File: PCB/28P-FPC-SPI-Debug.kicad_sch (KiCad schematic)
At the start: 33 parts, among them J1 Conn_01x08, J3 SFV24R-1STBE1HLF, Q1 Si1308EDL, Q2 AO3401A, Q3 S8050, U1 RT9193-33GB, U2 TXB0108PW

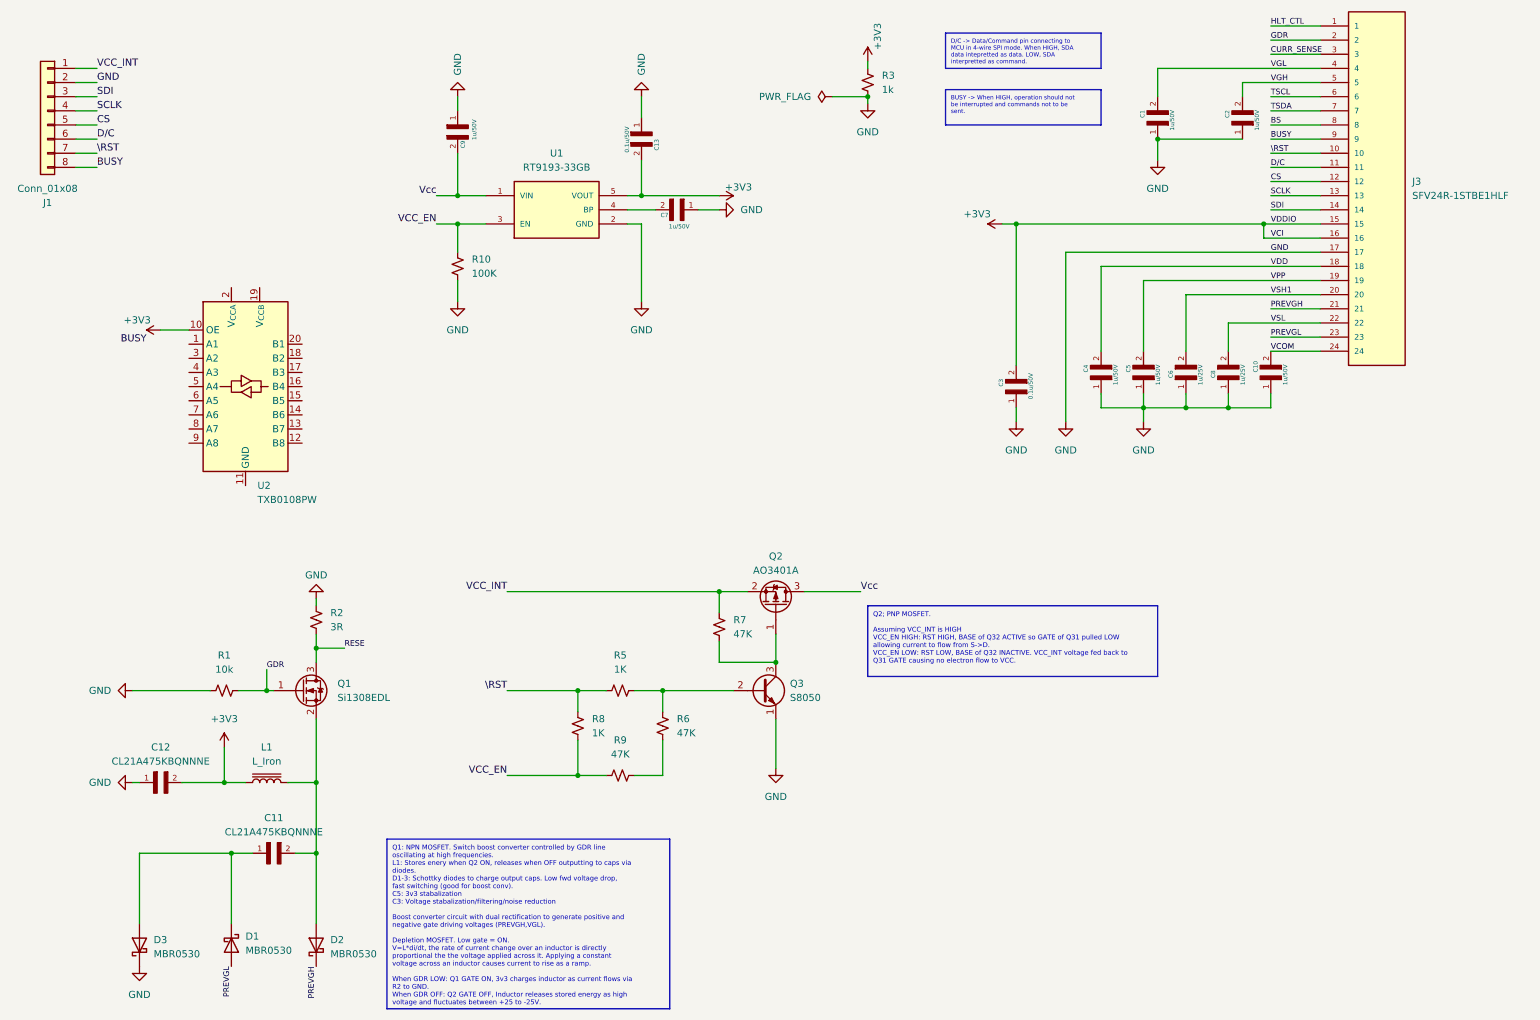
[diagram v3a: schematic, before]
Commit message: Added nets for TXB018PW. Resized PCB to size of 2.13in e-paper display with ~5mm excess on edges. Questionable part placement start.
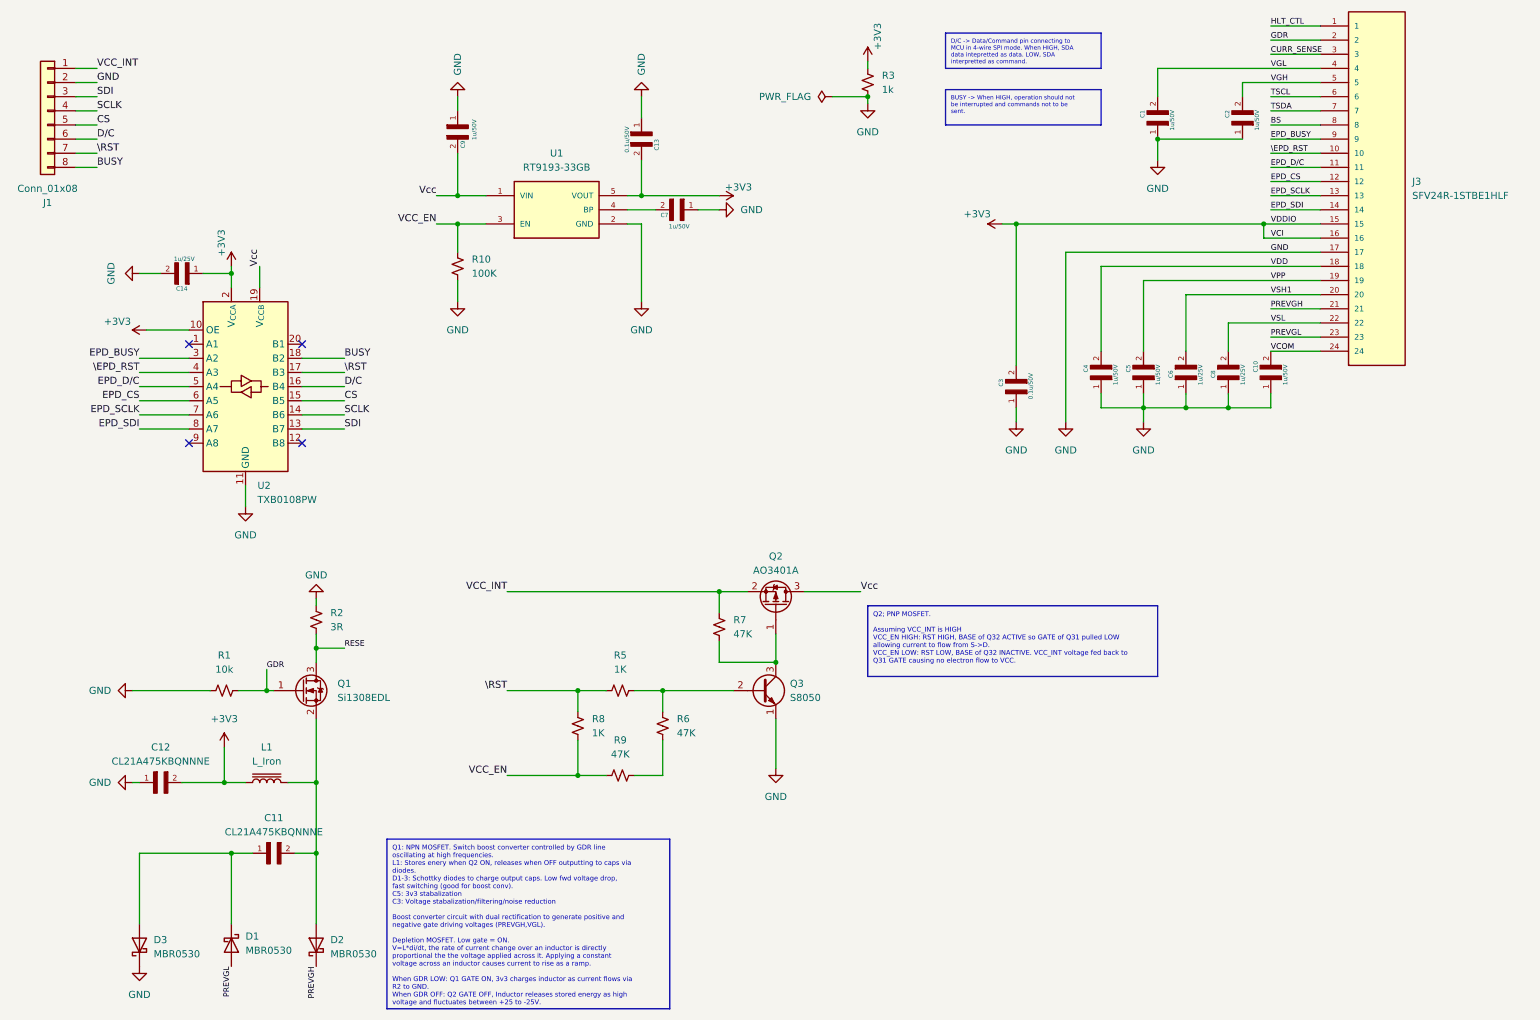
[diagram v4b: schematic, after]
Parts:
- added C14: 1u/25V, capacitors-cam:CAPC1608X90N, symbol Capacitors:CL10B105KA8NNNC
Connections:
- net +3V3: now also U2.2 (V_{CCA}), C14.1
- net BUSY: now also U2.18 (B2); no longer J3.9
- net CS: now also U2.15 (B5); no longer J3.12
- net D/C: now also U2.16 (B4); no longer J3.11
- net GND: now also U2.11 (GND), C14.2
- net SCLK: now also U2.14 (B6); no longer J3.13
- net SDI: now also U2.13 (B7); no longer J3.14
- net Vcc: now also U2.19 (V_{CCB})
- net \RST: now also U2.17 (B3); no longer J3.10
- net EPD_BUSY: now reaches U2.3 (A2)
- net EPD_BUSY: now also J3.9
- net \EPD_RST: now reaches U2.4 (A3)
- net \EPD_RST: now also J3.10
- net EPD_D/C: now reaches U2.5 (A4)
- net EPD_D/C: now also J3.11
- net EPD_CS: now reaches U2.6 (A5)
- net EPD_CS: now also J3.12
- net EPD_SCLK: now reaches U2.7 (A6)
- net EPD_SCLK: now also J3.13
- net EPD_SDI: now reaches U2.8 (A7)
- net EPD_SDI: now also J3.14
- no-connect marks 0 -> 4

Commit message: track placement
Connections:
- net VCC_EN: now also R9.1; no longer R9.2
- net VCC_INT: now also Q2.3 (D); no longer Q2.2 (S)
- net Vcc: now also Q2.2 (S); no longer Q2.3 (D)
- net at R6.1: now also R9.2; no longer R9.1
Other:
- moved on the sheet: Q2, R9
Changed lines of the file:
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@@
 	(symbol
 		(lib_id "Transistor_FET:AO3401A")
-		(at 149.86 120.65 270)
-		(mirror x)
-		(unit 1)
-		(exclude_from_sim no)
-		(in_bom yes)
-		(on_board yes)
-		(dnp no)
-		(fields_autoplaced yes)
+		(at 149.86 120.65 90)
+		(unit 1)
+		(exclude_from_sim no)
+		(in_bom yes)
+		(on_board yes)
+		(dnp no)
 		(property "Reference" "Q2"
 			(at 149.86 111.76 90)
@@
 		)
 		(property "Footprint" "Package_TO_SOT_SMD:SOT-23"
-			(at 147.955 115.57 0)
+			(at 151.765 115.57 0)
 			(effects
 				(font
@@
 		)
 		(property "Datasheet" "http://www.aosmd.com/pdfs/datasheet/AO3401A.pdf"
-			(at 146.05 115.57 0)
+			(at 153.67 115.57 0)
 			(effects
 				(font
@@
 	(symbol
 		(lib_id "Device:R_Small_US")
-		(at 121.92 151.13 270)
-		(unit 1)
-		(exclude_from_sim no)
-		(in_bom yes)
-		(on_board yes)
-		(dnp no)
-		(fields_autoplaced yes)
+		(at 121.92 151.13 90)
+		(mirror x)
+		(unit 1)
+		(exclude_from_sim no)
+		(in_bom yes)
+		(on_board yes)
+		(dnp no)
 		(property "Reference" "R9"
 			(at 121.92 144.78 90)

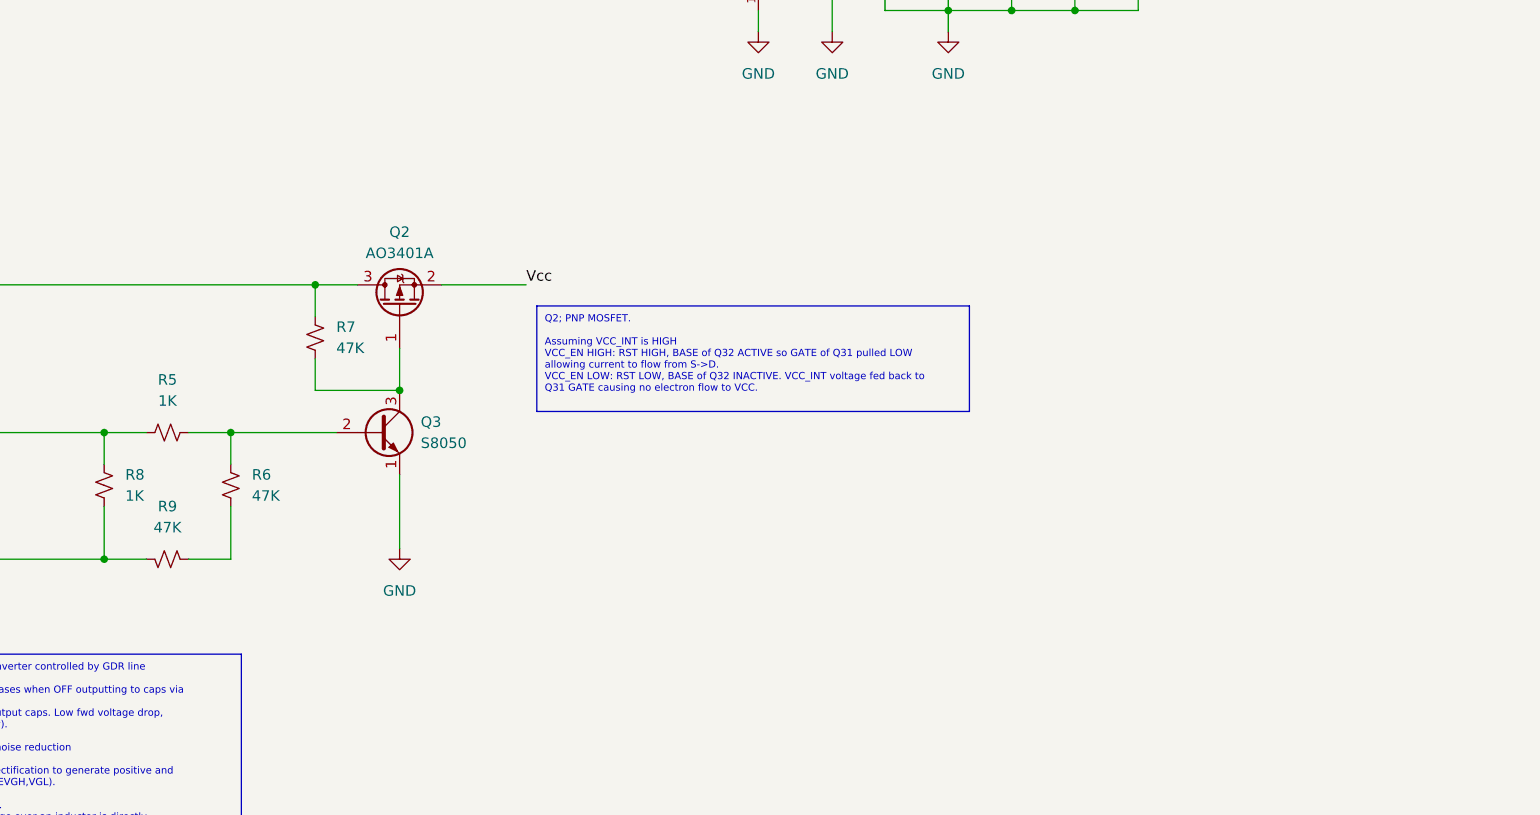
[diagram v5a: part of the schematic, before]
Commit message: Added breakout 28pin header for debugging. Track cleanup. Changed 0603 footprint due to clearance violations. Increased board size to fit header.
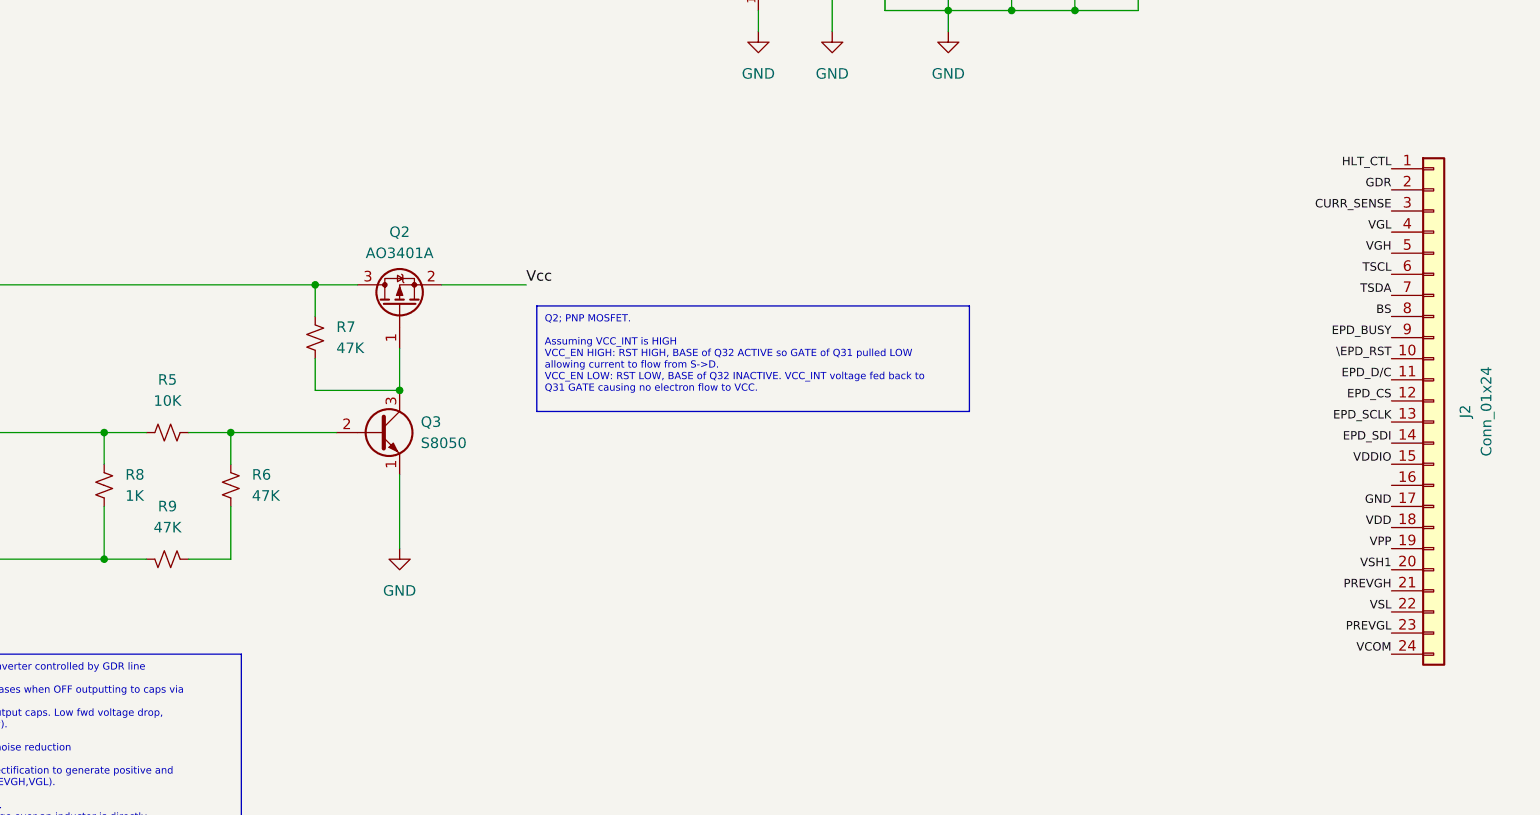
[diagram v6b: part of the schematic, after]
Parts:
- added J2: Conn_01x24, Connector_PinHeader_2.54mm:PinHeader_2x12_P2.54mm_Vertical, symbol Connector_Generic:Conn_01x24
- R1, R10, R2, R3, R6, R7, R8, R9: footprint Resistor_SMD:R_0201_0603Metric -> Resistor_SMD:R_0603_1608Metric_Pad0.98x0.95mm_HandSolder
- R5: value 1K -> 10K; footprint Resistor_SMD:R_0201_0603Metric -> Resistor_SMD:R_0603_1608Metric_Pad0.98x0.95mm_HandSolder
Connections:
- net +3V3: now also J2.15 (Pin_15)
- net BS: now also J2.8 (Pin_8)
- net CURR_SENSE: now also J2.3 (Pin_3)
- net EPD_BUSY: now also J2.9 (Pin_9)
- net EPD_CS: now also J2.12 (Pin_12)
- net EPD_D/C: now also J2.11 (Pin_11)
- net EPD_SCLK: now also J2.13 (Pin_13)
- net EPD_SDI: now also J2.14 (Pin_14)
- net GDR: now also J2.2 (Pin_2)
- net GND: now also J2.17 (Pin_17)
- net HLT_CTL: now also J2.1 (Pin_1)
- net PREVGH: now also J2.21 (Pin_21)
- net PREVGL: now also J2.23 (Pin_23)
- net TSCL: now also J2.6 (Pin_6)
- net TSDA: now also J2.7 (Pin_7)
- net VCOM: now also J2.24 (Pin_24)
- net VDD: now also J2.18 (Pin_18)
- net VGH: now also J2.5 (Pin_5)
- net VGL: now also J2.4 (Pin_4)
- net VPP: now also J2.19 (Pin_19)
- net VSH1: now also J2.20 (Pin_20)
- net VSL: now also J2.22 (Pin_22)
- net \EPD_RST: now also J2.10 (Pin_10)

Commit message: Moved some parts. Cleared ERC errors and warnings. Ready?
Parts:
- renumbered R7 to R10, R10 to R11, R8 to R6, R5 to R7, R6 to R8
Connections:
- net VCC_INT: now also Q2.2 (S); no longer Q2.3 (D)
- net Vcc: now also Q2.3 (D); no longer Q2.2 (S)
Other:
- moved on the sheet: Q2
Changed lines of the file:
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@@
 	(symbol
 		(lib_id "Transistor_FET:AO3401A")
-		(at 149.86 120.65 90)
+		(at 149.86 120.65 270)
+		(mirror x)
 		(unit 1)
 		(exclude_from_sim no)
@@
 		)
 		(property "Footprint" "Package_TO_SOT_SMD:SOT-23"
-			(at 151.765 115.57 0)
+			(at 147.955 115.57 0)
 			(effects
 				(font
@@
 		)
 		(property "Datasheet" "http://www.aosmd.com/pdfs/datasheet/AO3401A.pdf"
-			(at 153.67 115.57 0)
+			(at 146.05 115.57 0)
 			(effects
 				(font
@@
 		(dnp no)
 		(fields_autoplaced yes)
-		(property "Reference" "R6"
+		(property "Reference" "R8"
 			(at 132.08 140.9699 0)
 			(effects
@@
 			(project "28P-FPC-SPI-Debug"
 				(path "/301bb37e-82b1-4eff-97df-faf63e991923"
-					(reference "R6")
+					(reference "R8")
 					(unit 1)
 				)
@@
 		(dnp no)
 		(fields_autoplaced yes)
-		(property "Reference" "R8"
+		(property "Reference" "R6"
 			(at 116.84 140.9699 0)
 			(effects
@@
 			(project "28P-FPC-SPI-Debug"
 				(path "/301bb37e-82b1-4eff-97df-faf63e991923"
-					(reference "R8")
+					(reference "R6")
 					(unit 1)
 				)
@@
 		(dnp no)
 		(fields_autoplaced yes)
-		(property "Reference" "R7"
+		(property "Reference" "R10"
 			(at 142.24 123.1899 0)
 			(effects
@@
 			(project "28P-FPC-SPI-Debug"
 				(path "/301bb37e-82b1-4eff-97df-faf63e991923"
-					(reference "R7")
+					(reference "R10")
 					(unit 1)
 				)
@@
 		(dnp no)
 		(fields_autoplaced yes)
-		(property "Reference" "R10"
+		(property "Reference" "R11"
 			(at 95.25 58.4199 0)
 			(effects
@@
 			(project "28P-FPC-SPI-Debug"
 				(path "/301bb37e-82b1-4eff-97df-faf63e991923"
-					(reference "R10")
+					(reference "R11")
 					(unit 1)
 				)
@@
 		(dnp no)
 		(fields_autoplaced yes)
-		(property "Reference" "R5"
+		(property "Reference" "R7"
 			(at 121.92 129.54 90)
 			(effects
@@
 			(project "28P-FPC-SPI-Debug"
 				(path "/301bb37e-82b1-4eff-97df-faf63e991923"
-					(reference "R5")
-					(unit 1)
-				)
+					(reference "R7")
+					(unit 1)
+				)
